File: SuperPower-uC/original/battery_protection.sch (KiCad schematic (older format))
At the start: 8 parts, among them J1 JST_PH_S2B_thru, Q1 DMN2019UTS, U1 AP9101CK6-AYTRG1

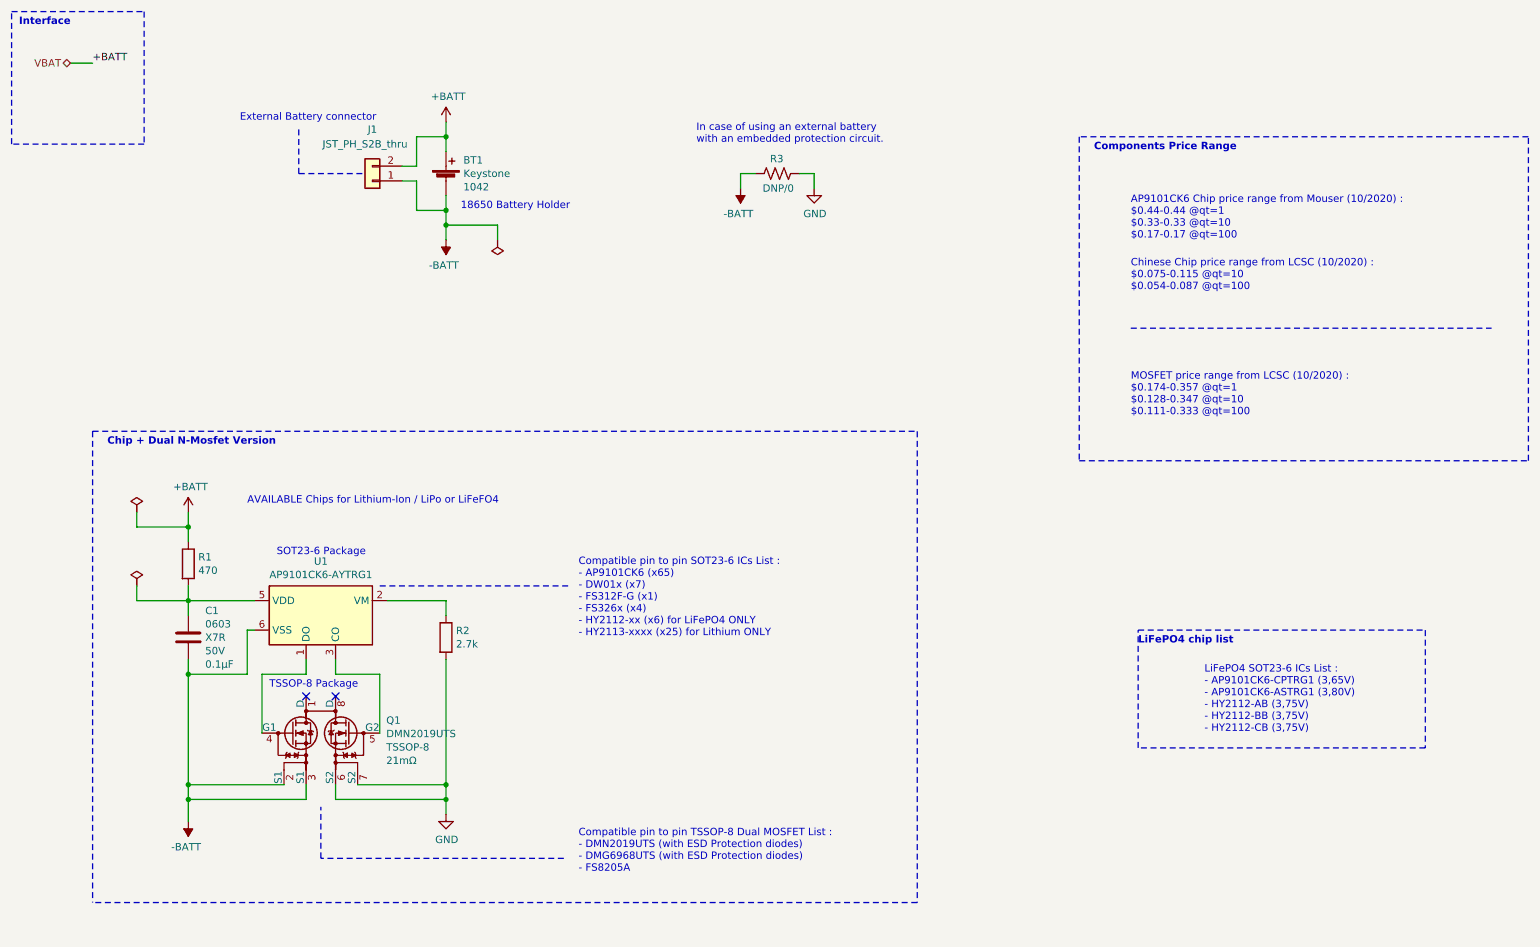
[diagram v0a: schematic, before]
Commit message: Update NTC Connector & USB-C Library path
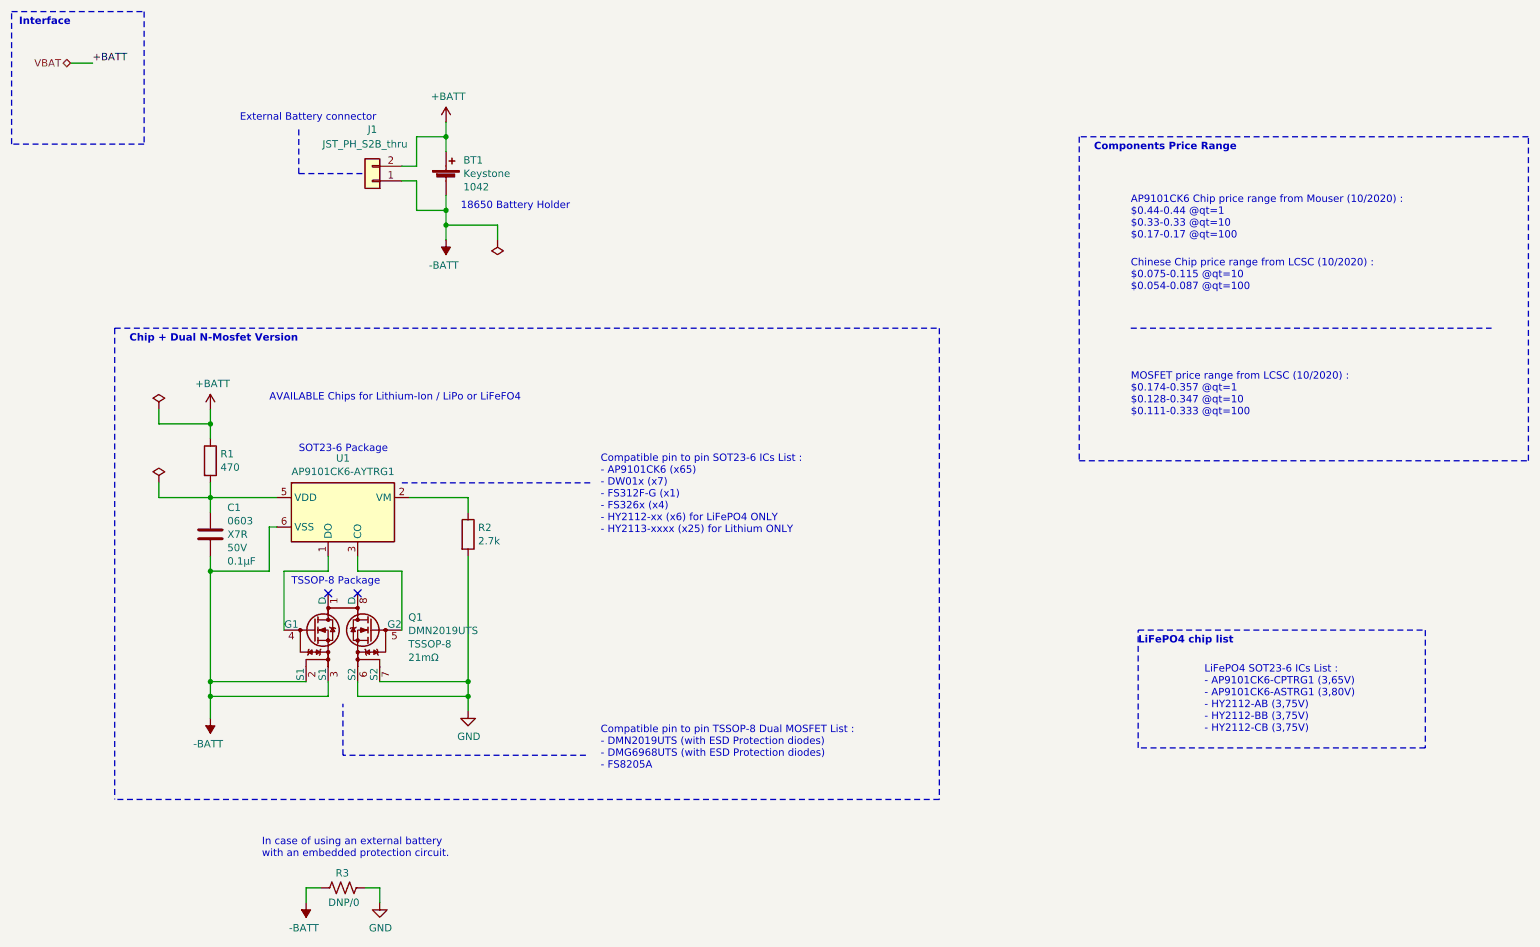
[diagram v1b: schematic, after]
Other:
- moved on the sheet: C1, Q1, R1, R2, R3, U1

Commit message: Updated footprints and fixed issues
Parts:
- BT1: footprint Battery:BatteryHolder_Keystone_1042_1x18650 -> Battery_Holders:Keystone_1042_1x18650
- J1: footprint Connector_JST:JST_PH_S2B-PH-K_1x02_P2.00mm_Horizontal -> Connectors_JST:JST_PH_S2B-PH-K_02x2.00mm_Angled
- U1: footprint Package_TO_SOT_SMD:SOT-23-6 -> TO_SOT_Packages_SMD:SOT-23-6
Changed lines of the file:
@@
 F 0 "U1" H 2800 4317 50  0000 C CNN
 F 1 "AP9101CK6-AYTRG1" H 2800 4226 50  0000 C CNN
-F 2 "Package_TO_SOT_SMD:SOT-23-6" H 2750 3950 50  0001 C CNN
+F 2 "TO_SOT_Packages_SMD:SOT-23-6" H 2750 3950 50  0001 C CNN
 F 3 "https://www.diodes.com/assets/Datasheets/AP9101C.pdf" H 2800 4000 50  0001 C CNN
 F 4 "https://octopart.com/ap9101ck6-aytrg1-diodes+inc.-77041826?r=sp" H 2800 3950 50  0001 C CNN "Octopart_link"
@@
 F 0 "J1" H 3000 1350 50  0000 C CNN
 F 1 "JST_PH_S2B_thru" H 3050 1450 50  0000 C CNN
-F 2 "Connector_JST:JST_PH_S2B-PH-K_1x02_P2.00mm_Horizontal" H 3000 1700 50  0001 C CNN
+F 2 "Connectors_JST:JST_PH_S2B-PH-K_02x2.00mm_Angled" H 3000 1700 50  0001 C CNN
 F 3 "http://www.jst-mfg.com/product/pdf/eng/ePH.pdf" H 3000 1700 50  0001 C CNN
 F 4 "JST" H 3000 1700 50  0001 C CNN "Mfr_name"
@@
 F 0 "BT1" H 3618 1841 50  0000 L CNN
 F 1 "Battery_Cell_Holder_18650_SMT_1042" H 3600 1700 50  0001 L CNN
-F 2 "Battery:BatteryHolder_Keystone_1042_1x18650" V 3500 1760 50  0001 C CNN
+F 2 "Battery_Holders:Keystone_1042_1x18650" V 3500 1760 50  0001 C CNN
 F 3 "https://www.keyelco.com/product-pdf.cfm?p=918" V 3500 1760 50  0001 C CNN
 F 4 "Keystone" H 3618 1750 50  0000 L CNN "Mfr_name"

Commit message: reassigned most footprints
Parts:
- BT1: footprint Battery_Holders:Keystone_1042_1x18650 -> Battery:BatteryHolder_Keystone_1042_1x18650
- C1: footprint Capacitors_SMD:C_0805 -> Capacitor_SMD:C_0805_2012Metric
- J1: footprint Connectors_JST:JST_PH_S2B-PH-K_02x2.00mm_Angled -> Connector_JST:JST_PH_S2B-PH-K_1x02_P2.00mm_Horizontal
- R1, R2, R3: footprint Resistors_SMD:R_0603 -> Resistor_SMD:R_0603_1608Metric
- U1: footprint TO_SOT_Packages_SMD:SOT-23-6 -> Package_TO_SOT_SMD:SOT-23-6
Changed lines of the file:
@@
 F 0 "R1" H 1968 3646 50  0000 L CNN
 F 1 "470" H 1968 3555 50  0000 L CNN
-F 2 "Resistors_SMD:R_0603" V 1940 3590 50  0001 C CNN
+F 2 "Resistor_SMD:R_0603_1608Metric" V 1940 3590 50  0001 C CNN
 F 3 "~" H 1900 3600 50  0001 C CNN
 	1    1900 3600
@@
 F 0 "R2" H 3718 4146 50  0000 L CNN
 F 1 "2.7k" H 3718 4055 50  0000 L CNN
-F 2 "Resistors_SMD:R_0603" V 3690 4090 50  0001 C CNN
+F 2 "Resistor_SMD:R_0603_1608Metric" V 3690 4090 50  0001 C CNN
 F 3 "~" H 3650 4100 50  0001 C CNN
 	1    3650 4100
@@
 F 0 "R3" V 2700 6450 50  0000 L CNN
 F 1 "DNP/0" V 2900 6400 50  0000 L CNN
-F 2 "Resistors_SMD:R_0603" V 2840 6490 50  0001 C CNN
+F 2 "Resistor_SMD:R_0603_1608Metric" V 2840 6490 50  0001 C CNN
 F 3 "~" H 2800 6500 50  0001 C CNN
 	1    2800 6500
@@
 F 0 "U1" H 2800 4317 50  0000 C CNN
 F 1 "AP9101CK6-AYTRG1" H 2800 4226 50  0000 C CNN
-F 2 "TO_SOT_Packages_SMD:SOT-23-6" H 2750 3950 50  0001 C CNN
+F 2 "Package_TO_SOT_SMD:SOT-23-6" H 2750 3950 50  0001 C CNN
 F 3 "https://www.diodes.com/assets/Datasheets/AP9101C.pdf" H 2800 4000 50  0001 C CNN
 F 4 "https://octopart.com/ap9101ck6-aytrg1-diodes+inc.-77041826?r=sp" H 2800 3950 50  0001 C CNN "Octopart_link"
@@
 F 0 "J1" H 3000 1350 50  0000 C CNN
 F 1 "JST_PH_S2B_thru" H 3050 1450 50  0000 C CNN
-F 2 "Connectors_JST:JST_PH_S2B-PH-K_02x2.00mm_Angled" H 3000 1700 50  0001 C CNN
+F 2 "Connector_JST:JST_PH_S2B-PH-K_1x02_P2.00mm_Horizontal" H 3000 1700 50  0001 C CNN
 F 3 "http://www.jst-mfg.com/product/pdf/eng/ePH.pdf" H 3000 1700 50  0001 C CNN
 F 4 "JST" H 3000 1700 50  0001 C CNN "Mfr_name"
@@
 F 0 "C1" H 2015 4282 50  0000 L CNN
 F 1 "CC0603JRX7R9BB104" H 1925 4000 50  0001 L CNN
-F 2 "Capacitors_SMD:C_0805" H 1938 3950 50  0001 C CNN
+F 2 "Capacitor_SMD:C_0805_2012Metric" H 1938 3950 50  0001 C CNN
 F 3 "https://www.yageo.com/upload/media/product/productsearch/datasheet/mlcc/UPY-GPHC_X7R_6.3V-to-50V_20.pdf" H 1900 4100 50  0001 C CNN
 F 4 "Yageo" H 1900 4100 50  0001 C CNN "Mfr_name"
@@
 F 0 "BT1" H 3618 1841 50  0000 L CNN
 F 1 "Battery_Cell_Holder_18650_SMT_1042" H 3600 1700 50  0001 L CNN
-F 2 "Battery_Holders:Keystone_1042_1x18650" V 3500 1760 50  0001 C CNN
+F 2 "Battery:BatteryHolder_Keystone_1042_1x18650" V 3500 1760 50  0001 C CNN
 F 3 "https://www.keyelco.com/product-pdf.cfm?p=918" V 3500 1760 50  0001 C CNN
 F 4 "Keystone" H 3618 1750 50  0000 L CNN "Mfr_name"

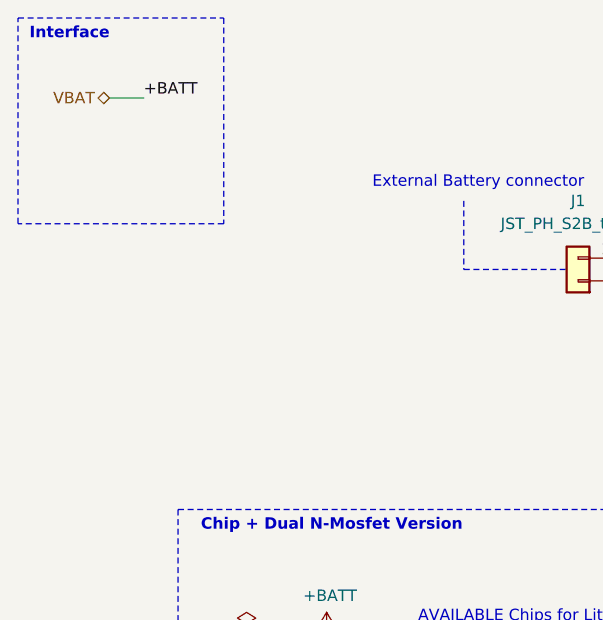
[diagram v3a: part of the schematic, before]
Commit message: Add test points to the interface
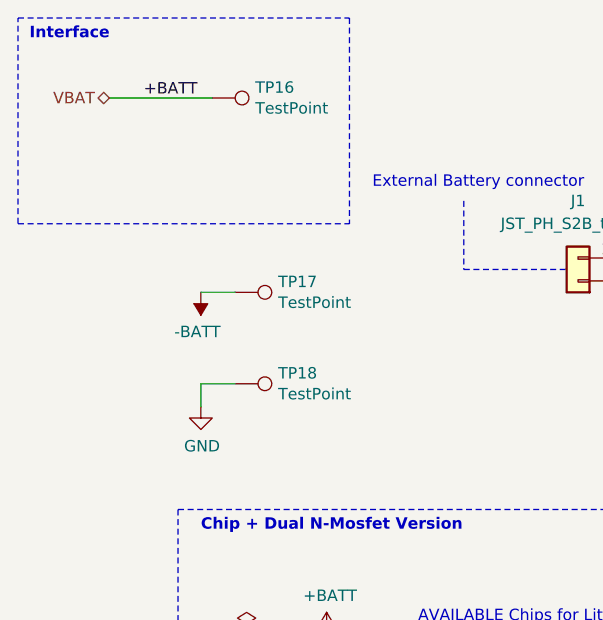
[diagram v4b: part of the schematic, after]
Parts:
- added TP16, TP17, TP18: TestPoint, TestPoint:TestPoint_Pad_D1.0mm, symbol Connector:TestPoint
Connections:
- net +BATT: now also TP16.1
- net -BATT: now also TP17.1
- net GND: now also TP18.1
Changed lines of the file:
@@
 Wire Notes Line
 	3200 3750 4500 3750
-Wire Wire Line
-	950  900  1100 900
 Text Label 1100 900  0    50   ~ 0
 +BATT
@@
 Interface
 Wire Notes Line
-	550  550  1450 550
-Wire Notes Line
-	1450 550  1450 1450
-Wire Notes Line
-	1450 1450 550  1450
+	2000 550  2000 1450
 Wire Notes Line
 	550  1450 550  550
@@
 	1    0    0    -1
 $EndComp
+Wire Notes Line
+	550  1450 2000 1450
+Wire Notes Line
+	550  550  2000 550
+$Comp
+L Connector:TestPoint TP16
+U 1 1 5FD97859
+P 1400 900
+F 0 "TP16" V 1354 1088 50  0000 L CNN
+F 1 "TestPoint" V 1445 1088 50  0000 L CNN
+F 2 "TestPoint:TestPoint_Pad_D1.0mm" H 1600 900 50  0001 C CNN
+F 3 "~" H 1600 900 50  0001 C CNN
+	1    1400 900
+	0    1    1    0
+$EndComp
+Wire Wire Line
+	950  900  1400 900
+$Comp
+L Connector:TestPoint TP17
+U 1 1 5FD99F7F
+P 1500 1750
+F 0 "TP17" V 1454 1938 50  0000 L CNN
+F 1 "TestPoint" V 1545 1938 50  0000 L CNN
+F 2 "TestPoint:TestPoint_Pad_D1.0mm" H 1700 1750 50  0001 C CNN
+F 3 "~" H 1700 1750 50  0001 C CNN
+	1    1500 1750
+	0    1    1    0
+$EndComp
+$Comp
+L power:-BATT #PWR0119
+U 1 1 5FD9A456
+P 1350 1750
+F 0 "#PWR0119" H 1350 1600 50  0001 C CNN
+F 1 "-BATT" H 1365 1923 50  0000 C CNN
+F 2 "" H 1350 1750 50  0001 C CNN
+F 3 "" H 1350 1750 50  0001 C CNN
+	1    1350 1750
+	-1   0    0    1
+$EndComp
+Wire Wire Line
+	1500 1750 1350 1750
+$Comp
+L Connector:TestPoint TP18
+U 1 1 5FDA33F6
+P 1500 2150
+F 0 "TP18" V 1454 2338 50  0000 L CNN
+F 1 "TestPoint" V 1545 2338 50  0000 L CNN
+F 2 "TestPoint:TestPoint_Pad_D1.0mm" H 1700 2150 50  0001 C CNN
+F 3 "~" H 1700 2150 50  0001 C CNN
+	1    1500 2150
+	0    1    1    0
+$EndComp
+$Comp
+L power:GND #PWR0120
+U 1 1 5FDA3698
+P 1350 2250
+F 0 "#PWR0120" H 1350 2000 50  0001 C CNN
+F 1 "GND" H 1355 2077 50  0000 C CNN
+F 2 "" H 1350 2250 50  0001 C CNN
+F 3 "" H 1350 2250 50  0001 C CNN
+	1    1350 2250
+	1    0    0    -1
+$EndComp
+Wire Wire Line
+	1500 2150 1350 2150
+Wire Wire Line
+	1350 2150 1350 2250
 $EndSCHEMATC
